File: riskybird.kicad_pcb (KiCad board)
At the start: 2 copper layers, 78 parts, among them J1 USB_B_Micro, J2 Conn_01x02, J3 Conn_01x02, J4 Conn_01x02, J5 Conn_01x02, Q5 DNBT8105-7, Q6 DNBT8105-7, SW1 SW_SPST, SW2 SW_SPST, SW3 SW_SPST, U1 MCP73831-2-OT, U2 MPU-9150, U3 TPS2113A, U4 LP2985-3.0, U5 MPL3115A2, U6 ESP32-C3-WROOM-02, U8 FT231XS

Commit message: before switching IMU to BMI088
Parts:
- moved J1 41.4 mm to (86.3, 95.4)
- moved FID1 39.9 mm to (100.0, 100.0)
- moved U6 36.7 mm to (110.6, 100.0)
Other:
- board outline added: 58.3 x 58.3 mm

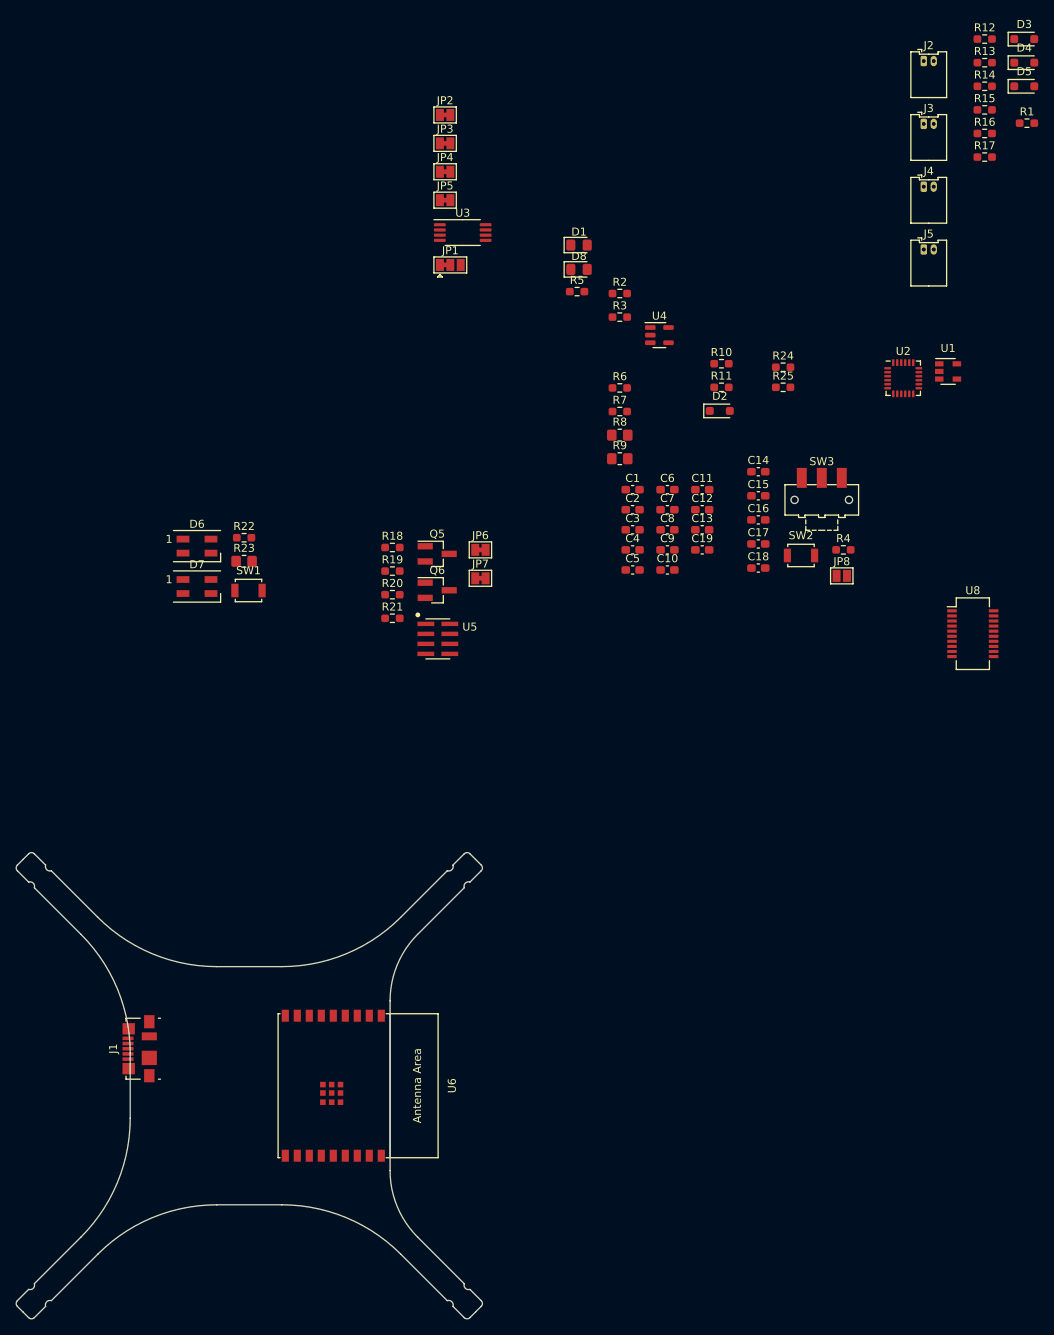
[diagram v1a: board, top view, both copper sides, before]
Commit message: add new BMI088 IMU
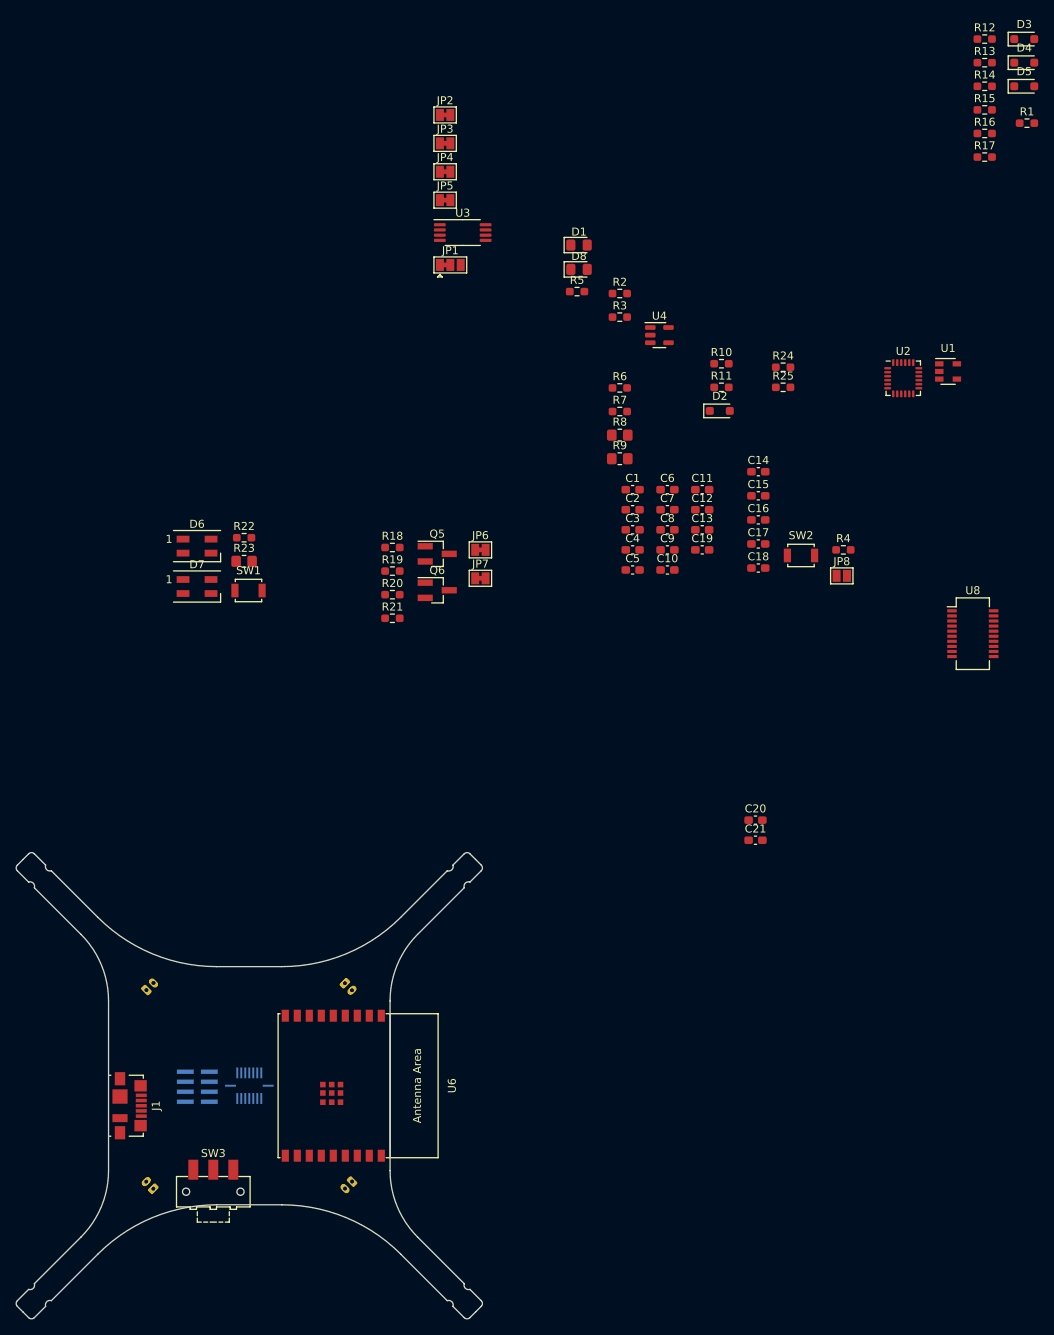
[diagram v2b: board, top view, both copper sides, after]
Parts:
- added C20: 10n, Capacitor_SMD:C_0603_1608Metric_Pad1.08x0.95mm_HandSolder, F.Cu at (163.3, 66.8)
- added C21: 4.7u, Capacitor_SMD:C_0603_1608Metric_Pad1.08x0.95mm_HandSolder, F.Cu at (163.3, 69.3)
- added U7: BMI088, riskybird:BMI088_Handsolder, B.Cu at (100.0, 100.0)
- J2, J3, J4, J5, U5: moved to B.Cu
- moved J3 164.3 mm to (88.0, 112.9), turned to 135 degrees
- moved J2 157.2 mm to (112.8, 112.0), turned to -135 degrees
- moved J4 139.7 mm to (87.1, 88.0), turned to 45 degrees
- moved J5 116.8 mm to (111.9, 87.2), turned to -45 degrees
- moved SW3 115.2 mm to (95.5, 113.2)
- moved U5 63.5 mm to (93.5, 100.1), turned to 180 degrees
- moved J1 7.24 mm to (85.0, 102.5), turned to -90 degrees
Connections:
- U6 pad 10: unconnected-(U6-GPIO10-Pad10) -> /INT1_BARO
- U6 pad 13: /INT_IMU -> /INT_ACC
- U6 pad 14: /INT1_BARO -> /INT_GYR
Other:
- outline, holes or cut-outs redrawn

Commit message: update footprints, begin placement
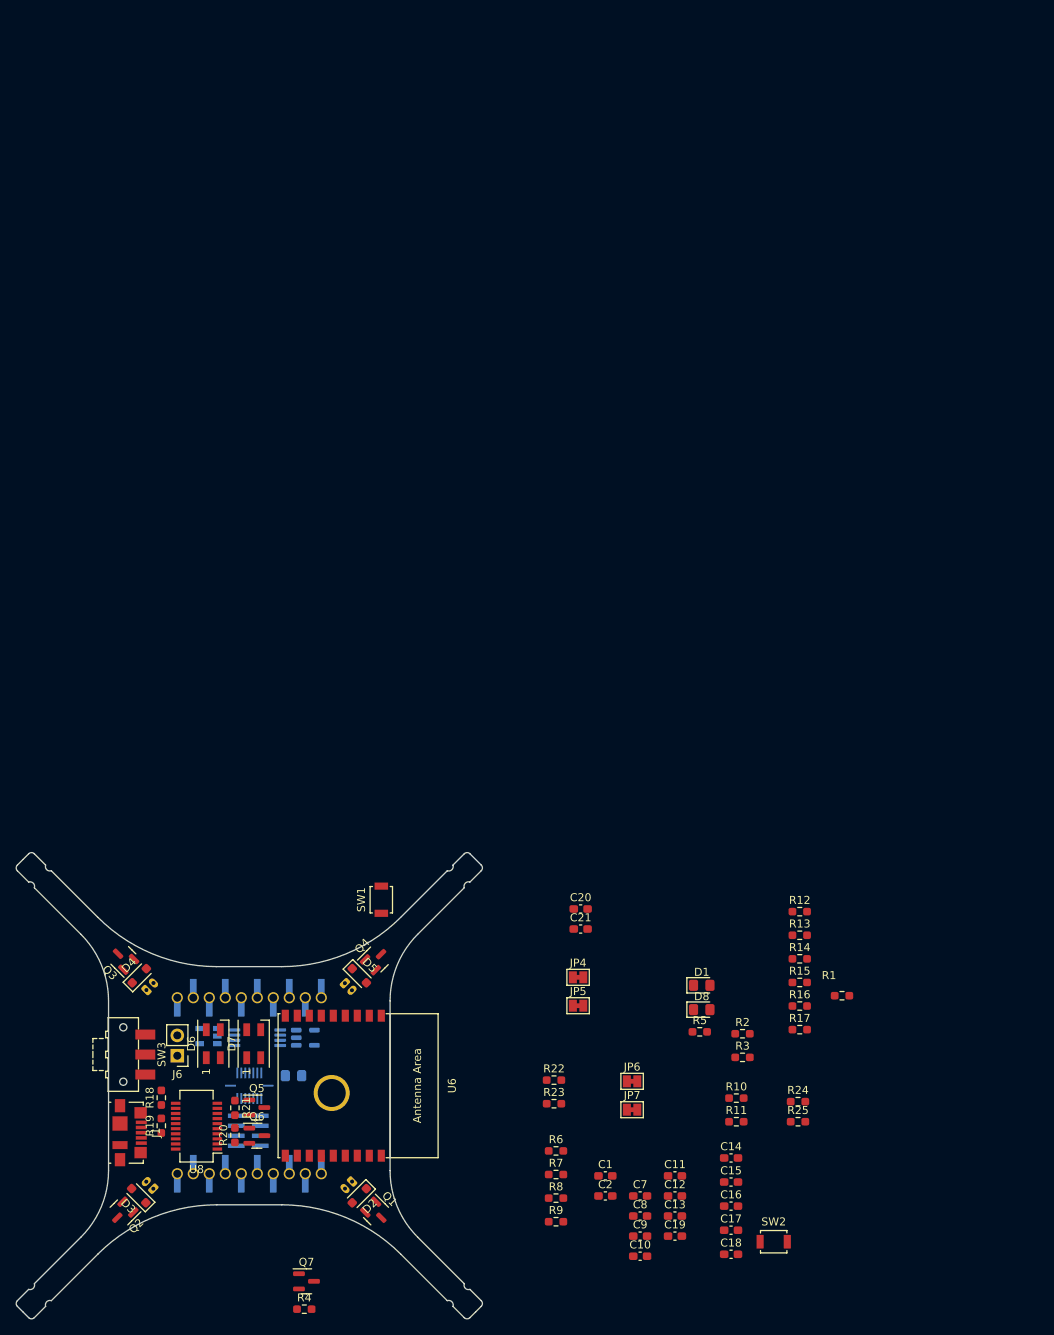
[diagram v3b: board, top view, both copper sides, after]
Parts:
- removed C3, C5: 0.1u, Capacitor_SMD:C_0603_1608Metric_Pad1.08x0.95mm_HandSolder
- removed C4: 10n, Capacitor_SMD:C_0603_1608Metric_Pad1.08x0.95mm_HandSolder
- removed C6: 2.2n, Capacitor_SMD:C_0603_1608Metric_Pad1.08x0.95mm_HandSolder
- removed JP1: SolderJumper_3_Bridged12, Jumper:SolderJumper-3_P1.3mm_Bridged12_Pad1.0x1.5mm
- removed JP2, JP3: SolderJumper_2_Bridged, Jumper:SolderJumper-2_P1.3mm_Bridged_Pad1.0x1.5mm
- removed JP8: SolderJumper_2_Open, Jumper:SolderJumper-2_P1.3mm_Open_Pad1.0x1.5mm
- removed U2: MPU-9150, Sensor_Motion:InvenSense_QFN-24_4x4mm_P0.5mm
- added J6: Conn_01x02, Connector_PinHeader_2.54mm:PinHeader_1x02_P2.54mm_Vertical, F.Cu at (91.0, 96.2)
- added J7: Conn_01x10, riskybird:PinHeader_1x10_P2.00mm_Vertical_SMD_Pin1Right_THT, B.Cu at (100.0, 111.0)
- added J8: Conn_01x10, riskybird:PinHeader_1x10_P2.00mm_Vertical_SMD_Pin1Right_THT, B.Cu at (100.0, 89.0)
- added L1: 1uH, Inductor_SMD:L_0805_2012Metric_Pad1.15x1.40mm_HandSolder, B.Cu at (105.5, 98.8)
- added Q1: SI2302, Package_TO_SOT_SMD:SOT-23, F.Cu at (115.8, 115.8)
- added Q2: SI2302, Package_TO_SOT_SMD:SOT-23, F.Cu at (84.2, 115.8)
- added Q3: SI2302, Package_TO_SOT_SMD:SOT-23, F.Cu at (84.3, 84.2)
- added Q4: SI2302, Package_TO_SOT_SMD:SOT-23, F.Cu at (115.8, 84.2)
- added Q7: Q_NMOS_GSD, Package_TO_SOT_SMD:SOT-23, F.Cu at (107.1, 124.5)
- Q5, Q6: footprint Package_TO_SOT_SMD:SOT-23_Handsoldering -> Package_TO_SOT_SMD:SOT-23
- R23, R8, R9: footprint Resistor_SMD:R_0805_2012Metric_Pad1.20x1.40mm_HandSolder -> Resistor_SMD:R_0603_1608Metric_Pad0.98x0.95mm_HandSolder
- R4: value 100k -> 10k
- U1, U3, U4: moved to B.Cu
- moved D3 182.1 mm to (86.2, 113.7), turned to 135 degrees
- moved D4 158.9 mm to (86.2, 86.2), turned to 45 degrees
- moved D5 138.8 mm to (113.8, 86.2), turned to -45 degrees
- moved U1 124.3 mm to (94.9, 93.8), turned to 180 degrees
- moved R4 116.4 mm to (106.9, 127.9)
- moved U8 114.9 mm to (93.4, 105.1), turned to 180 degrees
- moved R15 111.5 mm to (168.8, 87.1)
- moved R16 111.5 mm to (168.8, 90.0)
- moved R1 111.5 mm to (174.1, 88.8)
- moved R12 111.5 mm to (168.8, 78.2)
- moved R13 111.5 mm to (168.8, 81.2)
- moved R14 111.5 mm to (168.8, 84.1)
- moved R17 111.5 mm to (168.8, 93.0)
- moved D2 108.0 mm to (113.8, 113.8), turned to -135 degrees
- moved U3 103.9 mm to (101.0, 94.0)
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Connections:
- C19 pad 1: VCOM -> Net-(SW3-B)
- R4 pad 1: /VEN_D -> VCOM
- SW3 pad 1: /VEN_D -> VCOM
- SW3 pad 2: VCOM -> Net-(SW3-B)
- U1 pad 3: /VBAT -> +BATT
- U3 pad 7: VCOM -> Net-(SW3-B)
- U4 pad 3: /VEN_D -> VCOM
- U6 pad 17: unconnected-(U6-GPIO1/ADC1_CH1/XTAL_32K_N-Pad17) -> /OW

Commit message: finish initial placement draft
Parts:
- C1, C10, C11, C12, C14, C15, C16, C17, C18, C19, C2, C20, C21, C7, C8, C9, JP4, JP5, Q7, R1, R2, R22, R23, R24, R25, R3, R4, R5, R6, R7, R8, R9: moved to B.Cu
- moved R1 90.2 mm to (84.1, 95.0), turned to 180 degrees
- moved R13 84.1 mm to (91.4, 114.0), turned to 90 degrees
- moved R12 83.9 mm to (92.9, 114.0), turned to -90 degrees
- moved R15 77.6 mm to (91.2, 86.0), turned to -90 degrees
- moved R14 76.1 mm to (92.7, 86.0), turned to 90 degrees
- moved R3 74.2 mm to (87.5, 99.0)
- moved C19 71.6 mm to (83.5, 102.4), turned to -90 degrees
- moved SW2 70.5 mm to (104.6, 84.0), turned to 90 degrees
- moved R2 63.5 mm to (98.8, 84.2), turned to 90 degrees
- moved C13 62.4 mm to (93.1, 99.5)
- moved C1 62.2 mm to (84.1, 96.5), turned to 180 degrees
- moved C18 62.0 mm to (104.3, 94.3), turned to -90 degrees
- moved R16 61.7 mm to (107.2, 86.0), turned to 90 degrees
- moved C11 60.9 mm to (95.3, 92.3), turned to 180 degrees
- moved R17 60.5 mm to (108.7, 86.0), turned to -90 degrees
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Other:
- outline, holes or cut-outs redrawn

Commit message: start routing
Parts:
- moved R4 9.95 mm to (107.9, 106.2), turned to -90 degrees
- moved Q7 6.38 mm to (110.3, 106.0), turned to 90 degrees
- moved JP6 3.34 mm to (99.0, 97.2), turned to 0 degrees
- moved R25 2.82 mm to (112.9, 106.2), turned to 90 degrees
- moved C18 1.70 mm to (102.6, 94.3)
- moved R22 1.70 mm to (108.7, 94.3)
- moved R23 1.70 mm to (104.1, 94.3)
- moved R8 1.70 mm to (107.2, 94.3)
- moved R9 1.70 mm to (105.6, 94.3)
- moved C12 1.69 mm to (101.1, 94.3), turned to 90 degrees
- moved D1 1.60 mm to (98.7, 85.8)
- moved D8 1.60 mm to (101.0, 85.8)
- moved C8 1.42 mm to (96.4, 102.5), turned to -90 degrees
- moved JP7 1.33 mm to (99.0, 99.7), turned to 0 degrees
- moved SW1 1.30 mm to (95.1, 85.4)
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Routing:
- net VDD: track 0.00 -> 56.3 mm
- net /RGB_CTRL: track 0.00 -> 55.2 mm, vias 0 -> 3
- net /CHIP_EN: track 0.00 -> 43.7 mm, vias 0 -> 3
- net +5V: track 0.00 -> 41.9 mm, vias 0 -> 2
- net /SCL: track 0.00 -> 38.9 mm, vias 0 -> 1
- net +BATT: track 0.00 -> 33.3 mm
- net /SDA: track 0.00 -> 30.6 mm, vias 0 -> 1
- net /MOTOR3: track 0.00 -> 28.0 mm
- net VDDA: track 0.00 -> 24.6 mm
- net /MOTOR2: track 0.00 -> 21.5 mm
- net Net-(JP6-A): track 0.00 -> 14.9 mm
- net Net-(D1-K): track 0.00 -> 14.6 mm, vias 0 -> 1
- net /GPIO9: track 0.00 -> 12.8 mm, vias 0 -> 1
- net VCOM: track 0.00 -> 9.40 mm
- net Net-(Q1-G): track 0.00 -> 9.35 mm
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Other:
- board text added: "BOOT"
- board text added: "CHG"
- board text added: "PWR"
- board text added: "RST"

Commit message: almost done routing
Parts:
- removed C7: 10u, Capacitor_SMD:C_0603_1608Metric_Pad1.08x0.95mm_HandSolder
- removed C8: 100n, Capacitor_SMD:C_0603_1608Metric_Pad1.08x0.95mm_HandSolder
- removed C9: 0.1u, Capacitor_SMD:C_0603_1608Metric_Pad1.08x0.95mm_HandSolder
- removed JP4, JP5, JP7: SolderJumper_2_Bridged, Jumper:SolderJumper-2_P1.3mm_Bridged_Pad1.0x1.5mm
- added C3: 100n, Capacitor_SMD:C_0603_1608Metric_Pad1.08x0.95mm_HandSolder, B.Cu at (102.6, 105.7)
- added C4: 100n, Capacitor_SMD:C_0603_1608Metric_Pad1.08x0.95mm_HandSolder, B.Cu at (96.5, 105.6)
- added C5: 0.1u, Capacitor_SMD:C_0603_1608Metric_Pad1.08x0.95mm_HandSolder, B.Cu at (104.9, 106.0)
- added C6: 0.1u, Capacitor_SMD:C_0603_1608Metric_Pad1.08x0.95mm_HandSolder, B.Cu at (112.2, 106.0)
- added JP1: SolderJumper_2_Bridged, Jumper:SolderJumper-2_P1.3mm_Bridged_Pad1.0x1.5mm, F.Cu at (127.2, 97.0)
- added JP2: SolderJumper_2_Bridged, Jumper:SolderJumper-2_P1.3mm_Bridged_Pad1.0x1.5mm, F.Cu at (127.2, 100.5)
- added U2: ~, riskybird:BMP390_Handsolder, B.Cu at (99.7, 105.6)
- added U9: ~, Package_TO_SOT_SMD:SOT-363_SC-70-6, B.Cu at (110.0, 106.0)
- JP6: footprint Jumper:SolderJumper-2_P1.3mm_Bridged_Pad1.0x1.5mm -> Jumper:SolderJumper-2_P1.3mm_Open_Pad1.0x1.5mm
- U5: value MPL3115A2 -> ~; footprint riskybird:MPL3115A2 -> Package_TO_SOT_SMD:SOT-363_SC-70-6
- moved R4 9.01 mm to (114.8, 100.4), turned to 180 degrees
- moved U5 7.23 mm to (107.1, 106.0), turned to -90 degrees
- moved Q7 5.63 mm to (115.0, 102.8), turned to 0 degrees
- moved R25 2.07 mm to (114.8, 105.4), turned to 180 degrees
- moved R24 0.81 mm to (114.8, 106.9), turned to 0 degrees
- moved D6 0.65 mm to (103.8, 115.3)
- moved D7 0.55 mm to (96.2, 115.1)
- turned D2 to 45 degrees
- turned D4 to -135 degrees
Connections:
- C10 pad 2: GND -> GNDD
- C11 pad 2: GND -> GNDD
- C12 pad 2: GND -> GNDA
- C13 pad 2: GND -> GNDD
- C14 pad 2: GND -> GNDD
- C15 pad 2: GND -> GNDD
- C16 pad 2: GND -> GNDD
- C17 pad 2: GND -> GNDD
- C18 pad 2: GND -> GNDD
- C20 pad 2: GND -> GNDA
- C21 pad 2: GND -> GNDA
- D6 pad 2: GND -> GNDD
- D7 pad 2: GND -> GNDD
- D8 pad 1: GND -> GNDD
- J2 pad 1: +BATT -> Net-(D2-A)
- J2 pad 2: Net-(D2-A) -> +BATT
- J4 pad 1: +BATT -> Net-(D4-A)
- J4 pad 2: Net-(D4-A) -> +BATT
- J7 pad 2: unconnected-(J7-Pin_2-Pad2) -> /SRXD
- J7 pad 3: unconnected-(J7-Pin_3-Pad3) -> /STXD
- JP6 pad 1: Net-(JP6-A) -> /FTRXD
- JP6 pad 2: /UORXD -> /U0RXD
- Q7 pad 2: GND -> GNDD
- R4 pad 2: GND -> GNDD
- SW1 pad 1: GND -> GNDD
- SW2 pad 1: GND -> GNDD
- U5 pad 1: VDDA -> /FTRXD
- U5 pad 2: Net-(U5-CAP) -> GNDD
- U5 pad 3: GND -> /SRXD
- U5 pad 4: VDDA -> /U0RXD
- U5 pad 5: Net-(JP4-B) -> VDD
- U5 pad 6: Net-(JP5-B) -> +5V
- U6 pad 10: /INT1_BARO -> /INT_BARO
- U6 pad 19: GND -> GNDD
- U6 pad 9: GND -> GNDD
- U7 pad 15: GND -> GNDA
- U7 pad 4: GND -> GNDA
- U7 pad 6: GND -> GNDA
- U8 pad 16: GND -> GNDD
- U8 pad 20: Net-(JP6-A) -> /FTRXD
- U8 pad 4: Net-(JP7-A) -> /U0TXD
- U8 pad 6: GND -> GNDD
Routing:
- net GND: track 0.00 -> 113.0 mm, vias 0 -> 8
- net GNDD: track 0.00 -> 95.5 mm, vias 0 -> 11
- net +BATT: track 33.3 -> 115.6 mm
- net VDD: track 56.3 -> 121.2 mm, vias 0 -> 4
- net GNDA: track 0.00 -> 35.1 mm, vias 0 -> 4
- net /FTRXD: track 0.00 -> 33.4 mm, vias 0 -> 1
- net /OW: track 0.00 -> 30.4 mm, vias 0 -> 2
- net /U0RXD: track 0.00 -> 27.1 mm, vias 0 -> 2
- net +5V: track 41.9 -> 69.0 mm, vias 2 -> 3
- net /U0TXD: track 0.00 -> 26.9 mm, vias 0 -> 3
- net VDDA: track 24.6 -> 46.3 mm, vias 0 -> 4
- net /STXD: track 0.00 -> 21.0 mm
- net /INT_GYR: track 3.92 -> 23.9 mm, vias 0 -> 1
- net Net-(JP6-A): track 14.9 -> 0.00 mm
- net VCOM: track 9.40 -> 21.9 mm, vias 0 -> 1
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
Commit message: minor changes
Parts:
- JP1, JP2: moved to B.Cu
- moved JP2 8.03 mm to (135.0, 98.4), turned to 180 degrees
- moved JP1 5.93 mm to (133.0, 98.4), turned to 180 degrees

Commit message: finish routing
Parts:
- removed C5, C6: 0.1u, Capacitor_SMD:C_0603_1608Metric_Pad1.08x0.95mm_HandSolder
- removed JP6: SolderJumper_2_Bridged, Jumper:SolderJumper-2_P1.3mm_Open_Pad1.0x1.5mm
- removed U5, U9: ~, Package_TO_SOT_SMD:SOT-363_SC-70-6
- added C7: 0.1u, Capacitor_SMD:C_0603_1608Metric_Pad1.08x0.95mm_HandSolder, B.Cu at (112.2, 106.0)
- added G***: LOGO, LOGO, B.Cu at (96.5, 116.0)
- added U10: 74LVC2G08, Package_SO:VSSOP-8_3.0x3.0mm_P0.65mm, B.Cu at (108.0, 105.8)
- JP1: footprint Jumper:SolderJumper-2_P1.3mm_Bridged_Pad1.0x1.5mm -> riskybird:shunt
- JP2: footprint Jumper:SolderJumper-2_P1.3mm_Bridged_Pad1.0x1.5mm -> riskybird:shunt; moved to F.Cu
- moved JP1 39.8 mm to (93.2, 96.0), turned to -90 degrees
- moved JP2 37.3 mm to (97.8, 96.8), turned to 0 degrees
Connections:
- J7 pad 2: /SRXD -> /U0RXD
- J7 pad 3: /STXD -> /U0TXD
- J8 pad 1: unconnected-(J8-Pin_1-Pad1) -> /U1TXD
- J8 pad 2: unconnected-(J8-Pin_2-Pad2) -> /U1RXD
- U6 pad 10: /INT_BARO -> /INT_ACC_GYR_BARO
- U6 pad 13: /INT_ACC -> /U1RXD
- U6 pad 14: /INT_GYR -> /U1TXD
- U8 pad 20: /FTRXD -> /U0RXD
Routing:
- net /FTRXD: track 33.4 -> 0.00 mm, vias 1 -> 0
- net GND: track 113.0 -> 139.7 mm, vias 8 -> 10
- net VCOM: track 21.9 -> 47.1 mm, vias 1 -> 2
- net /U1RXD: track 0.00 -> 23.3 mm, vias 0 -> 1
- net /U1TXD: track 0.00 -> 23.0 mm, vias 0 -> 1
- net /STXD: track 21.0 -> 0.00 mm
- net /GPIO9: track 12.4 -> 31.4 mm, vias 1 -> 3
- net Net-(SW3-B): track 7.73 -> 24.8 mm, vias 1 -> 2
- net GNDD: track 95.5 -> 112.3 mm
- net +5V: track 69.0 -> 55.1 mm
- net /INT_GYR: track 23.9 -> 13.9 mm, vias 1 -> 0
- net /INT_ACC: track 0.00 -> 9.56 mm, vias 0 -> 2
- net VDD: track 121.2 -> 112.7 mm, vias 4 -> 3
- net /SRXD: track 7.74 -> 0.00 mm
- net GNDA: track 35.1 -> 42.4 mm, vias 4 -> 6
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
